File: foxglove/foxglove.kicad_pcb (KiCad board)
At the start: 2 copper layers, 70.7 x 53.3 mm, 17 parts, among them J1 NEIGHBOR1, J2 NEIGHBOR2, J3 RJ45, J7 BONUS_ROW, P1 CONN_02X05, U1 SHIFTER1, U2 SHIFTER2, U3 SHIFTER3, U4 SHIFTER4, U5 SHIFTER5, U6 SHIFTER6, U7 SHIFTER7, U8 SHIFTER8

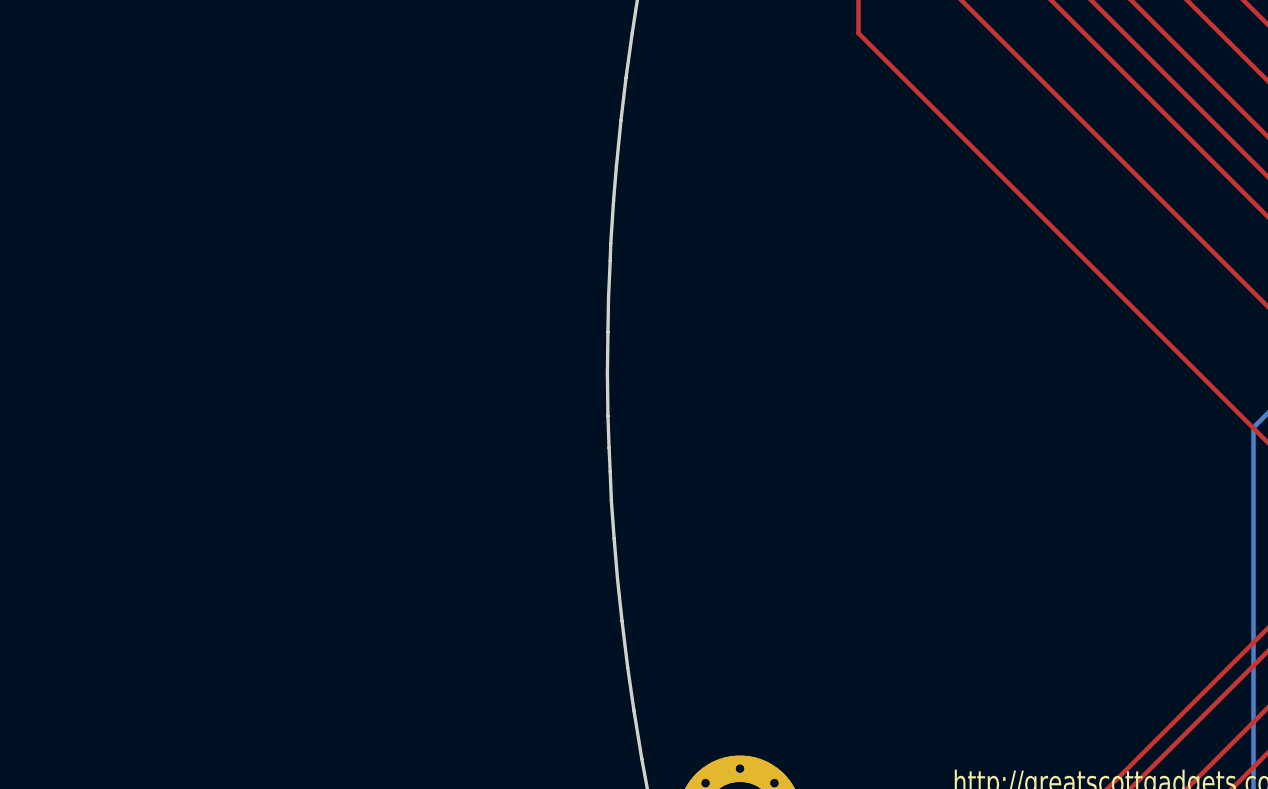
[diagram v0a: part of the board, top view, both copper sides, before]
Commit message: Added greenPAK and iCE40 to schematic, started routing power connections
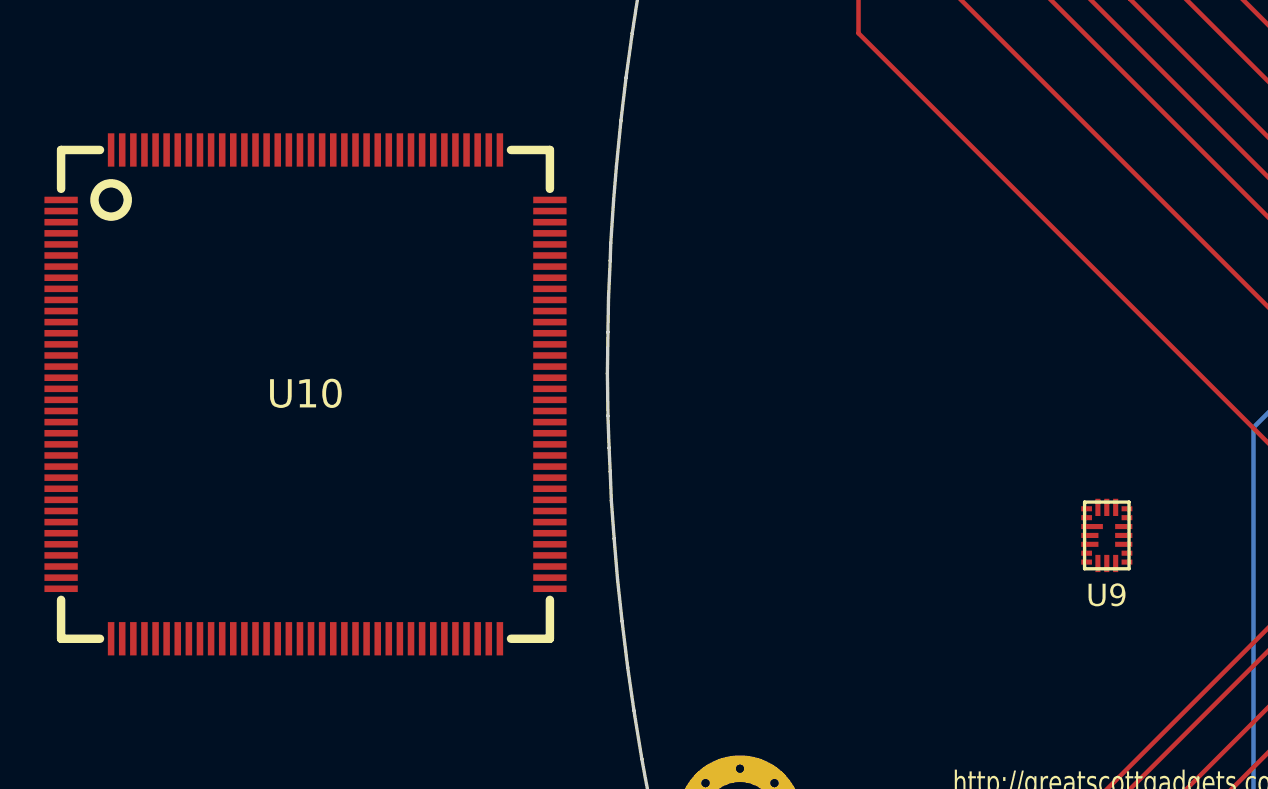
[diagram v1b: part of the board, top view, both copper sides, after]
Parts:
- added U10: iCE40HX4K, gsg-modules:LQFP144, F.Cu at (96.0, 96.5)
- added U9: SLG46621, gsg-modules:SLG46621, F.Cu at (132.1, 102.9)
